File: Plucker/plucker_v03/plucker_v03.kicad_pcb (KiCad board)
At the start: 2 copper layers, 79.1 x 79.4 mm, 13 parts, among them J1_BNC1 BNC5-J-P-GN-RA-BH2D, J2_BLACK1 Conn_01x01, J3_RED1 Conn_01x01, T1 GT07-110-013, U1 SL1002A600SP

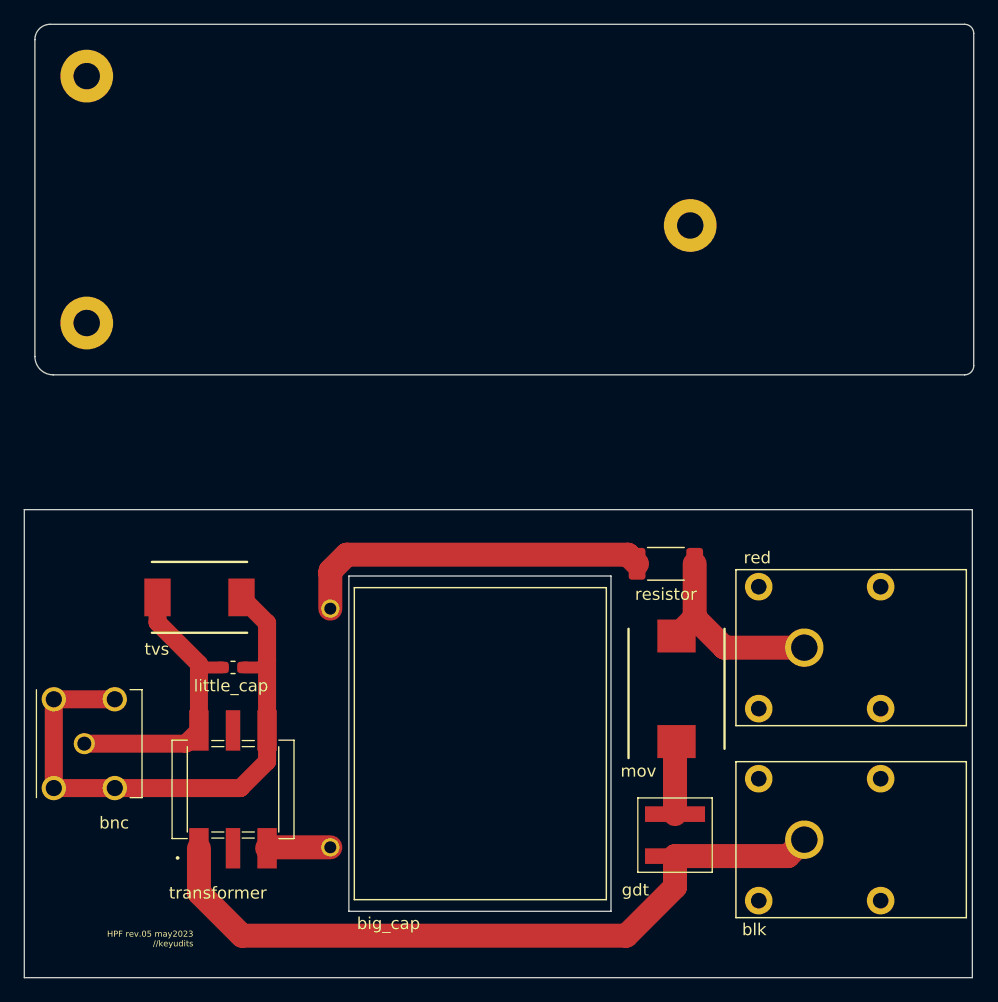
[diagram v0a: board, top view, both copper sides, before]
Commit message: assembled v03, added waveforms
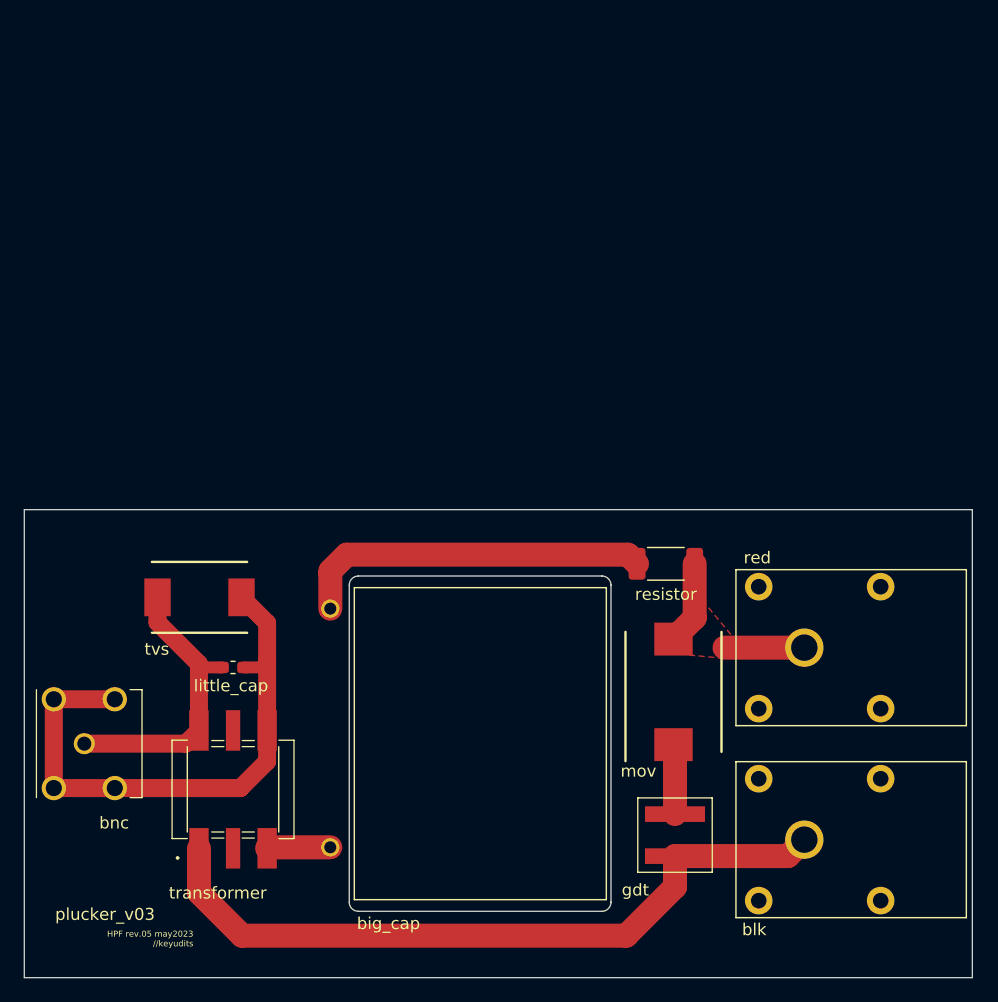
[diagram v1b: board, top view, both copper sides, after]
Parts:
- removed REF** (x3): MountingHole_2.2mm_M2_Pad, MountingHole:MountingHole_2.2mm_M2_Pad
- moved RV1 0.36 mm to (159.8, 100.6)
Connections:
- net Net-(J3_RED1-Pad1) renamed in
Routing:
- net in: track 16.8 -> 13.3 mm
- added copper zone on F.Cu, net in
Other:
- board size 79.1 x 79.4 mm -> 79 x 39 mm
- rule pad_to_mask_clearance: 0.05 -> 0
- board text added: "cutout this section please"
- board text added: "plucker_v03"
- board text removed: "cutout"
